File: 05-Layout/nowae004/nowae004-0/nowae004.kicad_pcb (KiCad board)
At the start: 2 copper layers, 150 x 68 mm, 801 parts, among them P1 SUPPLY IN, P2 MICROUSB, U2 FT230XS

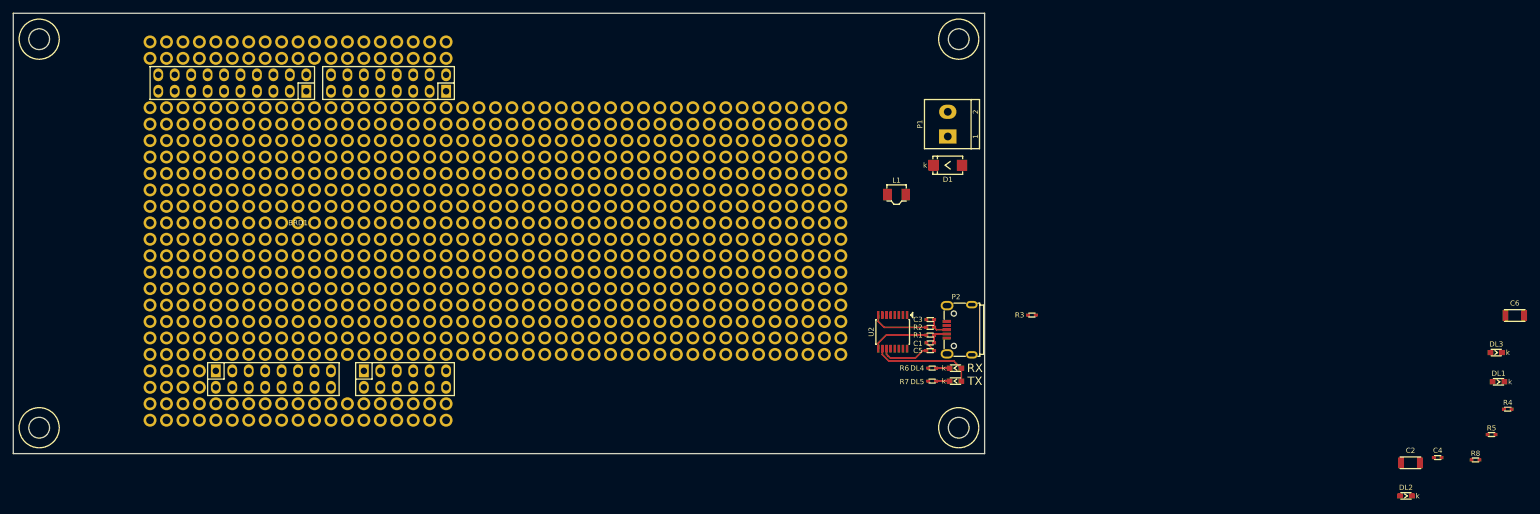
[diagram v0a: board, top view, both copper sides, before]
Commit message: NOWAE004: ended PCB development. TODO is fiducial, logos, license and hole in GND plane
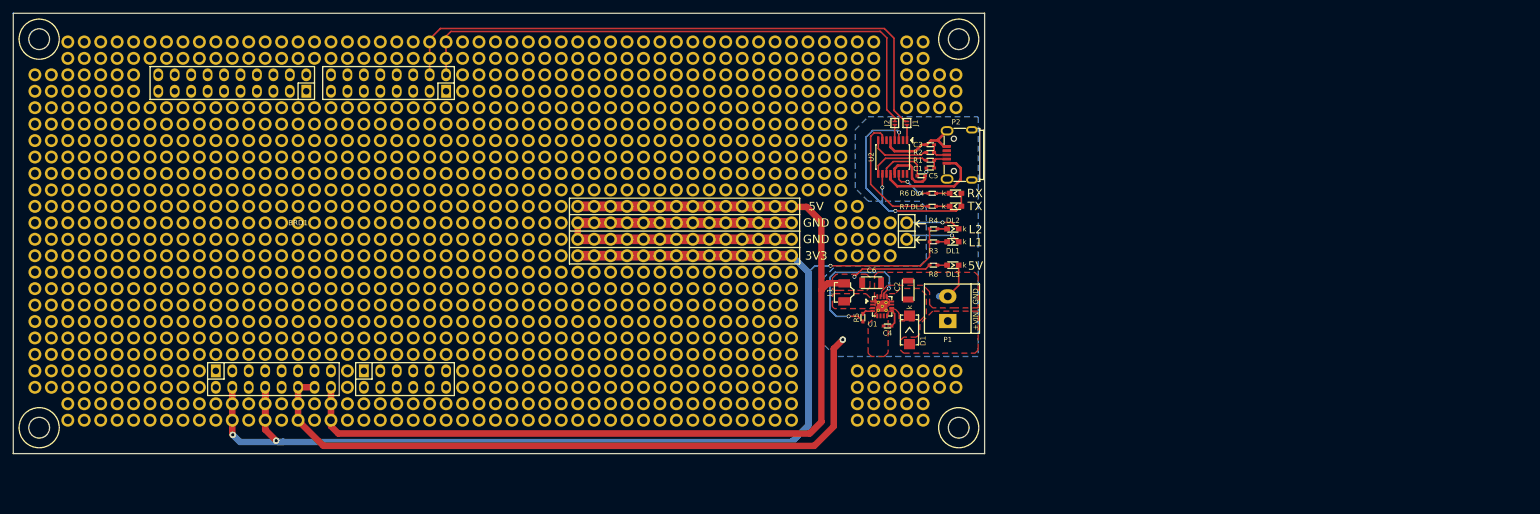
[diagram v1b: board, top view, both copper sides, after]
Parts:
- removed the VAL** at (177.8, 106.7)
- removed the VAL** at (177.8, 104.1)
- removed the VAL** at (177.8, 101.6)
- removed the VAL** at (177.8, 99.1)
- removed the VAL** at (177.8, 96.5)
- removed the VAL** at (177.8, 94.0)
- removed the VAL** at (175.3, 83.8)
- removed the VAL** at (175.3, 86.4)
- removed the VAL** at (175.3, 88.9)
- removed the VAL** at (175.3, 91.4)
- removed the VAL** at (175.3, 94.0)
- removed the VAL** at (175.3, 96.5)
- removed the VAL** at (175.3, 99.1)
- removed the VAL** at (175.3, 101.6)
- removed the VAL** at (175.3, 104.1)
- removed the VAL** at (175.3, 106.7)
- removed the VAL** at (172.7, 83.8)
- removed the VAL** at (172.7, 86.4)
- removed the VAL** at (172.7, 88.9)
- removed the VAL** at (172.7, 91.4)
- removed the VAL** at (172.7, 94.0)
- removed the VAL** at (172.7, 96.5)
- removed the VAL** at (172.7, 99.1)
- removed the VAL** at (172.7, 101.6)
- removed the VAL** at (172.7, 104.1)
- removed the VAL** at (172.7, 106.7)
- added J1: EN_SERIAL, MISC:JUMPERSMD-2, F.Cu at (188.0, 71.0)
- added J2: EN_SERIAL, MISC:JUMPERSMD-2, F.Cu at (186.1, 71.0)
- added P3: LED1, CONNECTOR:CONN-HOLE-1.2, F.Cu at (188.0, 88.9)
- added P4: LED2, CONNECTOR:CONN-HOLE-1.2, F.Cu at (188.0, 86.4)
- added U1: TPS62153, QFN:QFN16_3x3_0.5_16+1, F.Cu at (184.2, 99.2)
- added VAL**: CONN-HOLE-1.2, CONNECTOR:CONN-HOLE-1.2, F.Cu at (53.3, 106.7)
- added VAL**: CONN-HOLE-1.2, CONNECTOR:CONN-HOLE-1.2, F.Cu at (55.9, 106.7)
- added VAL**: CONN-HOLE-1.2, CONNECTOR:CONN-HOLE-1.2, F.Cu at (61.0, 91.4)
- added VAL**: CONN-HOLE-1.2, CONNECTOR:CONN-HOLE-1.2, F.Cu at (63.5, 86.4)
- added VAL**: CONN-HOLE-1.2, CONNECTOR:CONN-HOLE-1.2, F.Cu at (61.0, 88.9)
- added VAL**: CONN-HOLE-1.2, CONNECTOR:CONN-HOLE-1.2, F.Cu at (63.5, 88.9)
- added VAL**: CONN-HOLE-1.2, CONNECTOR:CONN-HOLE-1.2, F.Cu at (63.5, 91.4)
- added VAL**: CONN-HOLE-1.2, CONNECTOR:CONN-HOLE-1.2, F.Cu at (66.0, 86.4)
- added VAL**: CONN-HOLE-1.2, CONNECTOR:CONN-HOLE-1.2, F.Cu at (68.6, 88.9)
- added VAL**: CONN-HOLE-1.2, CONNECTOR:CONN-HOLE-1.2, F.Cu at (66.0, 91.4)
- added VAL**: CONN-HOLE-1.2, CONNECTOR:CONN-HOLE-1.2, F.Cu at (66.0, 88.9)
- added VAL**: CONN-HOLE-1.2, CONNECTOR:CONN-HOLE-1.2, F.Cu at (68.6, 86.4)
- added VAL**: CONN-HOLE-1.2, CONNECTOR:CONN-HOLE-1.2, F.Cu at (55.9, 94.0)
- added VAL**: CONN-HOLE-1.2, CONNECTOR:CONN-HOLE-1.2, F.Cu at (68.6, 91.4)
- added VAL**: CONN-HOLE-1.2, CONNECTOR:CONN-HOLE-1.2, F.Cu at (68.6, 94.0)
- added VAL**: CONN-HOLE-1.2, CONNECTOR:CONN-HOLE-1.2, F.Cu at (61.0, 94.0)
- added VAL**: CONN-HOLE-1.2, CONNECTOR:CONN-HOLE-1.2, F.Cu at (63.5, 94.0)
- added VAL**: CONN-HOLE-1.2, CONNECTOR:CONN-HOLE-1.2, F.Cu at (66.0, 94.0)
- added VAL**: CONN-HOLE-1.2, CONNECTOR:CONN-HOLE-1.2, F.Cu at (61.0, 104.1)
- added VAL**: CONN-HOLE-1.2, CONNECTOR:CONN-HOLE-1.2, F.Cu at (63.5, 101.6)
- added VAL**: CONN-HOLE-1.2, CONNECTOR:CONN-HOLE-1.2, F.Cu at (63.5, 104.1)
- added VAL**: CONN-HOLE-1.2, CONNECTOR:CONN-HOLE-1.2, F.Cu at (66.0, 101.6)
- added VAL**: CONN-HOLE-1.2, CONNECTOR:CONN-HOLE-1.2, F.Cu at (58.4, 104.1)
- added VAL**: CONN-HOLE-1.2, CONNECTOR:CONN-HOLE-1.2, F.Cu at (55.9, 99.1)
- added VAL**: CONN-HOLE-1.2, CONNECTOR:CONN-HOLE-1.2, F.Cu at (58.4, 99.1)
- added VAL**: CONN-HOLE-1.2, CONNECTOR:CONN-HOLE-1.2, F.Cu at (58.4, 101.6)
- added VAL**: CONN-HOLE-1.2, CONNECTOR:CONN-HOLE-1.2, F.Cu at (58.4, 94.0)
- added VAL**: CONN-HOLE-1.2, CONNECTOR:CONN-HOLE-1.2, F.Cu at (58.4, 96.5)
- added VAL**: CONN-HOLE-1.2, CONNECTOR:CONN-HOLE-1.2, F.Cu at (61.0, 96.5)
- added VAL**: CONN-HOLE-1.2, CONNECTOR:CONN-HOLE-1.2, F.Cu at (63.5, 96.5)
- added VAL**: CONN-HOLE-1.2, CONNECTOR:CONN-HOLE-1.2, F.Cu at (66.0, 96.5)
- added VAL**: CONN-HOLE-1.2, CONNECTOR:CONN-HOLE-1.2, F.Cu at (66.0, 99.1)
- added VAL**: CONN-HOLE-1.2, CONNECTOR:CONN-HOLE-1.2, F.Cu at (63.5, 99.1)
- added VAL**: CONN-HOLE-1.2, CONNECTOR:CONN-HOLE-1.2, F.Cu at (68.6, 101.6)
- added VAL**: CONN-HOLE-1.2, CONNECTOR:CONN-HOLE-1.2, F.Cu at (55.9, 96.5)
- added VAL**: CONN-HOLE-1.2, CONNECTOR:CONN-HOLE-1.2, F.Cu at (68.6, 99.1)
- added VAL**: CONN-HOLE-1.2, CONNECTOR:CONN-HOLE-1.2, F.Cu at (68.6, 96.5)
- added VAL**: CONN-HOLE-1.2, CONNECTOR:CONN-HOLE-1.2, F.Cu at (68.6, 104.1)
- added VAL**: CONN-HOLE-1.2, CONNECTOR:CONN-HOLE-1.2, F.Cu at (66.0, 106.7)
- added VAL**: CONN-HOLE-1.2, CONNECTOR:CONN-HOLE-1.2, F.Cu at (66.0, 104.1)
- added VAL**: CONN-HOLE-1.2, CONNECTOR:CONN-HOLE-1.2, F.Cu at (61.0, 101.6)
- added VAL**: CONN-HOLE-1.2, CONNECTOR:CONN-HOLE-1.2, F.Cu at (61.0, 99.1)
- added VAL**: CONN-HOLE-1.2, CONNECTOR:CONN-HOLE-1.2, F.Cu at (58.4, 109.2)
- added VAL**: CONN-HOLE-1.2, CONNECTOR:CONN-HOLE-1.2, F.Cu at (61.0, 109.2)
- added VAL**: CONN-HOLE-1.2, CONNECTOR:CONN-HOLE-1.2, F.Cu at (68.6, 106.7)
- added VAL**: CONN-HOLE-1.2, CONNECTOR:CONN-HOLE-1.2, F.Cu at (55.9, 101.6)
- added VAL**: CONN-HOLE-1.2, CONNECTOR:CONN-HOLE-1.2, F.Cu at (68.6, 109.2)
- added VAL**: CONN-HOLE-1.2, CONNECTOR:CONN-HOLE-1.2, F.Cu at (61.0, 106.7)
- added VAL**: CONN-HOLE-1.2, CONNECTOR:CONN-HOLE-1.2, F.Cu at (58.4, 106.7)
- added VAL**: CONN-HOLE-1.2, CONNECTOR:CONN-HOLE-1.2, F.Cu at (63.5, 106.7)
- added VAL**: CONN-HOLE-1.2, CONNECTOR:CONN-HOLE-1.2, F.Cu at (66.0, 109.2)
- added VAL**: CONN-HOLE-1.2, CONNECTOR:CONN-HOLE-1.2, F.Cu at (63.5, 109.2)
- added VAL**: CONN-HOLE-1.2, CONNECTOR:CONN-HOLE-1.2, F.Cu at (61.0, 111.8)
- added VAL**: CONN-HOLE-1.2, CONNECTOR:CONN-HOLE-1.2, F.Cu at (58.4, 111.8)
- added VAL**: CONN-HOLE-1.2, CONNECTOR:CONN-HOLE-1.2, F.Cu at (58.4, 114.3)
- added VAL**: CONN-HOLE-1.2, CONNECTOR:CONN-HOLE-1.2, F.Cu at (58.4, 116.8)
- added VAL**: CONN-HOLE-1.2, CONNECTOR:CONN-HOLE-1.2, F.Cu at (55.9, 109.2)
- added VAL**: CONN-HOLE-1.2, CONNECTOR:CONN-HOLE-1.2, F.Cu at (61.0, 116.8)
- added VAL**: CONN-HOLE-1.2, CONNECTOR:CONN-HOLE-1.2, F.Cu at (63.5, 111.8)
- added VAL**: CONN-HOLE-1.2, CONNECTOR:CONN-HOLE-1.2, F.Cu at (61.0, 114.3)
- added VAL**: CONN-HOLE-1.2, CONNECTOR:CONN-HOLE-1.2, F.Cu at (63.5, 114.3)
- added VAL**: CONN-HOLE-1.2, CONNECTOR:CONN-HOLE-1.2, F.Cu at (63.5, 116.8)
- added VAL**: CONN-HOLE-1.2, CONNECTOR:CONN-HOLE-1.2, F.Cu at (66.0, 111.8)
- added VAL**: CONN-HOLE-1.2, CONNECTOR:CONN-HOLE-1.2, F.Cu at (68.6, 114.3)
- added VAL**: CONN-HOLE-1.2, CONNECTOR:CONN-HOLE-1.2, F.Cu at (66.0, 116.8)
- added VAL**: CONN-HOLE-1.2, CONNECTOR:CONN-HOLE-1.2, F.Cu at (66.0, 114.3)
- added VAL**: CONN-HOLE-1.2, CONNECTOR:CONN-HOLE-1.2, F.Cu at (68.6, 111.8)
- added VAL**: CONN-HOLE-1.2, CONNECTOR:CONN-HOLE-1.2, F.Cu at (55.9, 111.8)
- added VAL**: CONN-HOLE-1.2, CONNECTOR:CONN-HOLE-1.2, F.Cu at (68.6, 116.8)
- added VAL**: CONN-HOLE-1.2, CONNECTOR:CONN-HOLE-1.2, F.Cu at (180.3, 91.4)
- added VAL**: CONN-HOLE-1.2, CONNECTOR:CONN-HOLE-1.2, F.Cu at (182.9, 91.4)
- added VAL**: CONN-HOLE-1.2, CONNECTOR:CONN-HOLE-1.2, F.Cu at (185.4, 91.4)
- added VAL**: CONN-HOLE-1.2, CONNECTOR:CONN-HOLE-1.2, F.Cu at (193.0, 63.5)
- added VAL**: CONN-HOLE-1.2, CONNECTOR:CONN-HOLE-1.2, F.Cu at (195.6, 68.6)
- added VAL**: CONN-HOLE-1.2, CONNECTOR:CONN-HOLE-1.2, F.Cu at (193.0, 66.0)
- added VAL**: CONN-HOLE-1.2, CONNECTOR:CONN-HOLE-1.2, F.Cu at (195.6, 66.0)
- added VAL**: CONN-HOLE-1.2, CONNECTOR:CONN-HOLE-1.2, F.Cu at (193.0, 68.6)
- added VAL**: CONN-HOLE-1.2, CONNECTOR:CONN-HOLE-1.2, F.Cu at (53.3, 88.9)
- added VAL**: CONN-HOLE-1.2, CONNECTOR:CONN-HOLE-1.2, F.Cu at (195.6, 63.5)
- added VAL**: CONN-HOLE-1.2, CONNECTOR:CONN-HOLE-1.2, F.Cu at (188.0, 58.4)
- added VAL**: CONN-HOLE-1.2, CONNECTOR:CONN-HOLE-1.2, F.Cu at (190.5, 58.4)
- added VAL**: CONN-HOLE-1.2, CONNECTOR:CONN-HOLE-1.2, F.Cu at (188.0, 61.0)
- added VAL**: CONN-HOLE-1.2, CONNECTOR:CONN-HOLE-1.2, F.Cu at (190.5, 61.0)
- added VAL**: CONN-HOLE-1.2, CONNECTOR:CONN-HOLE-1.2, F.Cu at (188.0, 63.5)
- added VAL**: CONN-HOLE-1.2, CONNECTOR:CONN-HOLE-1.2, F.Cu at (190.5, 68.6)
- added VAL**: CONN-HOLE-1.2, CONNECTOR:CONN-HOLE-1.2, F.Cu at (188.0, 66.0)
- added VAL**: CONN-HOLE-1.2, CONNECTOR:CONN-HOLE-1.2, F.Cu at (190.5, 66.0)
- added VAL**: CONN-HOLE-1.2, CONNECTOR:CONN-HOLE-1.2, F.Cu at (188.0, 68.6)
- added VAL**: CONN-HOLE-1.2, CONNECTOR:CONN-HOLE-1.2, F.Cu at (53.3, 91.4)
- added VAL**: CONN-HOLE-1.2, CONNECTOR:CONN-HOLE-1.2, F.Cu at (190.5, 63.5)
- added VAL**: CONN-HOLE-1.2, CONNECTOR:CONN-HOLE-1.2, F.Cu at (180.3, 61.0)
- added VAL**: CONN-HOLE-1.2, CONNECTOR:CONN-HOLE-1.2, F.Cu at (180.3, 63.5)
- added VAL**: CONN-HOLE-1.2, CONNECTOR:CONN-HOLE-1.2, F.Cu at (182.9, 63.5)
- added VAL**: CONN-HOLE-1.2, CONNECTOR:CONN-HOLE-1.2, F.Cu at (182.9, 58.4)
- added VAL**: CONN-HOLE-1.2, CONNECTOR:CONN-HOLE-1.2, F.Cu at (180.3, 58.4)
- added VAL**: CONN-HOLE-1.2, CONNECTOR:CONN-HOLE-1.2, F.Cu at (182.9, 61.0)
- added VAL**: CONN-HOLE-1.2, CONNECTOR:CONN-HOLE-1.2, F.Cu at (180.3, 66.0)
- added VAL**: CONN-HOLE-1.2, CONNECTOR:CONN-HOLE-1.2, F.Cu at (182.9, 68.6)
- added VAL**: CONN-HOLE-1.2, CONNECTOR:CONN-HOLE-1.2, F.Cu at (182.9, 66.0)
- added VAL**: CONN-HOLE-1.2, CONNECTOR:CONN-HOLE-1.2, F.Cu at (53.3, 81.3)
- added VAL**: CONN-HOLE-1.2, CONNECTOR:CONN-HOLE-1.2, F.Cu at (180.3, 68.6)
- added VAL**: CONN-HOLE-1.2, CONNECTOR:CONN-HOLE-1.2, F.Cu at (172.7, 58.4)
- added VAL**: CONN-HOLE-1.2, CONNECTOR:CONN-HOLE-1.2, F.Cu at (172.7, 61.0)
- added VAL**: CONN-HOLE-1.2, CONNECTOR:CONN-HOLE-1.2, F.Cu at (177.8, 58.4)
- added VAL**: CONN-HOLE-1.2, CONNECTOR:CONN-HOLE-1.2, F.Cu at (175.3, 61.0)
- added VAL**: CONN-HOLE-1.2, CONNECTOR:CONN-HOLE-1.2, F.Cu at (177.8, 61.0)
- added VAL**: CONN-HOLE-1.2, CONNECTOR:CONN-HOLE-1.2, F.Cu at (175.3, 58.4)
- added VAL**: CONN-HOLE-1.2, CONNECTOR:CONN-HOLE-1.2, F.Cu at (175.3, 63.5)
- added VAL**: CONN-HOLE-1.2, CONNECTOR:CONN-HOLE-1.2, F.Cu at (172.7, 63.5)
- added VAL**: CONN-HOLE-1.2, CONNECTOR:CONN-HOLE-1.2, F.Cu at (177.8, 63.5)
- added VAL**: CONN-HOLE-1.2, CONNECTOR:CONN-HOLE-1.2, F.Cu at (53.3, 104.1)
- added VAL**: CONN-HOLE-1.2, CONNECTOR:CONN-HOLE-1.2, F.Cu at (53.3, 78.7)
- added VAL**: CONN-HOLE-1.2, CONNECTOR:CONN-HOLE-1.2, F.Cu at (175.3, 66.0)
- added VAL**: CONN-HOLE-1.2, CONNECTOR:CONN-HOLE-1.2, F.Cu at (177.8, 66.0)
- added VAL**: CONN-HOLE-1.2, CONNECTOR:CONN-HOLE-1.2, F.Cu at (172.7, 66.0)
- added VAL**: CONN-HOLE-1.2, CONNECTOR:CONN-HOLE-1.2, F.Cu at (53.3, 76.2)
- added VAL**: CONN-HOLE-1.2, CONNECTOR:CONN-HOLE-1.2, F.Cu at (185.4, 86.4)
- added VAL**: CONN-HOLE-1.2, CONNECTOR:CONN-HOLE-1.2, F.Cu at (53.3, 86.4)
- added VAL**: CONN-HOLE-1.2, CONNECTOR:CONN-HOLE-1.2, F.Cu at (185.4, 88.9)
- added VAL**: CONN-HOLE-1.2, CONNECTOR:CONN-HOLE-1.2, F.Cu at (182.9, 88.9)
- added VAL**: CONN-HOLE-1.2, CONNECTOR:CONN-HOLE-1.2, F.Cu at (180.3, 83.8)
- added VAL**: CONN-HOLE-1.2, CONNECTOR:CONN-HOLE-1.2, F.Cu at (180.3, 86.4)
- added VAL**: CONN-HOLE-1.2, CONNECTOR:CONN-HOLE-1.2, F.Cu at (180.3, 88.9)
- added VAL**: CONN-HOLE-1.2, CONNECTOR:CONN-HOLE-1.2, F.Cu at (182.9, 86.4)
- added VAL**: CONN-HOLE-1.2, CONNECTOR:CONN-HOLE-1.2, F.Cu at (53.3, 83.8)
- added VAL**: CONN-HOLE-1.2, CONNECTOR:CONN-HOLE-1.2, F.Cu at (190.5, 114.3)
- added VAL**: CONN-HOLE-1.2, CONNECTOR:CONN-HOLE-1.2, F.Cu at (188.0, 116.8)
- added VAL**: CONN-HOLE-1.2, CONNECTOR:CONN-HOLE-1.2, F.Cu at (190.5, 116.8)
- added VAL**: CONN-HOLE-1.2, CONNECTOR:CONN-HOLE-1.2, F.Cu at (185.4, 116.8)
- added VAL**: CONN-HOLE-1.2, CONNECTOR:CONN-HOLE-1.2, F.Cu at (182.9, 114.3)
- added VAL**: CONN-HOLE-1.2, CONNECTOR:CONN-HOLE-1.2, F.Cu at (182.9, 109.2)
- added VAL**: CONN-HOLE-1.2, CONNECTOR:CONN-HOLE-1.2, F.Cu at (180.3, 116.8)
- added VAL**: CONN-HOLE-1.2, CONNECTOR:CONN-HOLE-1.2, F.Cu at (180.3, 114.3)
- added VAL**: CONN-HOLE-1.2, CONNECTOR:CONN-HOLE-1.2, F.Cu at (180.3, 111.8)
- added VAL**: CONN-HOLE-1.2, CONNECTOR:CONN-HOLE-1.2, F.Cu at (53.3, 73.7)
- added VAL**: CONN-HOLE-1.2, CONNECTOR:CONN-HOLE-1.2, F.Cu at (182.9, 116.8)
- added VAL**: CONN-HOLE-1.2, CONNECTOR:CONN-HOLE-1.2, F.Cu at (180.3, 109.2)
- added VAL**: CONN-HOLE-1.2, CONNECTOR:CONN-HOLE-1.2, F.Cu at (182.9, 111.8)
- added VAL**: CONN-HOLE-1.2, CONNECTOR:CONN-HOLE-1.2, F.Cu at (185.4, 114.3)
- added VAL**: CONN-HOLE-1.2, CONNECTOR:CONN-HOLE-1.2, F.Cu at (188.0, 111.8)
- added VAL**: CONN-HOLE-1.2, CONNECTOR:CONN-HOLE-1.2, F.Cu at (185.4, 111.8)
- added VAL**: CONN-HOLE-1.2, CONNECTOR:CONN-HOLE-1.2, F.Cu at (190.5, 111.8)
- added VAL**: CONN-HOLE-1.2, CONNECTOR:CONN-HOLE-1.2, F.Cu at (188.0, 114.3)
- added VAL**: CONN-HOLE-1.2, CONNECTOR:CONN-HOLE-1.2, F.Cu at (185.4, 109.2)
- added VAL**: CONN-HOLE-1.2, CONNECTOR:CONN-HOLE-1.2, F.Cu at (188.0, 109.2)
- added VAL**: CONN-HOLE-1.2, CONNECTOR:CONN-HOLE-1.2, F.Cu at (53.3, 68.6)
- added VAL**: CONN-HOLE-1.2, CONNECTOR:CONN-HOLE-1.2, F.Cu at (190.5, 109.2)
- added VAL**: CONN-HOLE-1.2, CONNECTOR:CONN-HOLE-1.2, F.Cu at (195.6, 111.8)
- added VAL**: CONN-HOLE-1.2, CONNECTOR:CONN-HOLE-1.2, F.Cu at (193.0, 111.8)
- added VAL**: CONN-HOLE-1.2, CONNECTOR:CONN-HOLE-1.2, F.Cu at (195.6, 109.2)
- added VAL**: CONN-HOLE-1.2, CONNECTOR:CONN-HOLE-1.2, F.Cu at (193.0, 109.2)
- added VAL**: CONN-HOLE-1.2, CONNECTOR:CONN-HOLE-1.2, F.Cu at (132.1, 109.2)
- added VAL**: CONN-HOLE-1.2, CONNECTOR:CONN-HOLE-1.2, F.Cu at (127.0, 114.3)
- added VAL**: CONN-HOLE-1.2, CONNECTOR:CONN-HOLE-1.2, F.Cu at (127.0, 111.8)
- added VAL**: CONN-HOLE-1.2, CONNECTOR:CONN-HOLE-1.2, F.Cu at (127.0, 109.2)
- added VAL**: CONN-HOLE-1.2, CONNECTOR:CONN-HOLE-1.2, F.Cu at (129.5, 109.2)
- added VAL**: CONN-HOLE-1.2, CONNECTOR:CONN-HOLE-1.2, F.Cu at (53.3, 71.1)
- added VAL**: CONN-HOLE-1.2, CONNECTOR:CONN-HOLE-1.2, F.Cu at (134.6, 116.8)
- added VAL**: CONN-HOLE-1.2, CONNECTOR:CONN-HOLE-1.2, F.Cu at (127.0, 116.8)
- added VAL**: CONN-HOLE-1.2, CONNECTOR:CONN-HOLE-1.2, F.Cu at (134.6, 114.3)
- added VAL**: CONN-HOLE-1.2, CONNECTOR:CONN-HOLE-1.2, F.Cu at (134.6, 111.8)
- added VAL**: CONN-HOLE-1.2, CONNECTOR:CONN-HOLE-1.2, F.Cu at (134.6, 109.2)
- added VAL**: CONN-HOLE-1.2, CONNECTOR:CONN-HOLE-1.2, F.Cu at (121.9, 116.8)
- added VAL**: CONN-HOLE-1.2, CONNECTOR:CONN-HOLE-1.2, F.Cu at (119.4, 116.8)
- added VAL**: CONN-HOLE-1.2, CONNECTOR:CONN-HOLE-1.2, F.Cu at (124.5, 116.8)
- added VAL**: CONN-HOLE-1.2, CONNECTOR:CONN-HOLE-1.2, F.Cu at (124.5, 114.3)
- added VAL**: CONN-HOLE-1.2, CONNECTOR:CONN-HOLE-1.2, F.Cu at (119.4, 114.3)
- added VAL**: CONN-HOLE-1.2, CONNECTOR:CONN-HOLE-1.2, F.Cu at (55.9, 78.7)
- added VAL**: CONN-HOLE-1.2, CONNECTOR:CONN-HOLE-1.2, F.Cu at (121.9, 114.3)
- added VAL**: CONN-HOLE-1.2, CONNECTOR:CONN-HOLE-1.2, F.Cu at (132.1, 111.8)
- added VAL**: CONN-HOLE-1.2, CONNECTOR:CONN-HOLE-1.2, F.Cu at (129.5, 111.8)
- added VAL**: CONN-HOLE-1.2, CONNECTOR:CONN-HOLE-1.2, F.Cu at (129.5, 116.8)
- added VAL**: CONN-HOLE-1.2, CONNECTOR:CONN-HOLE-1.2, F.Cu at (132.1, 114.3)
- added VAL**: CONN-HOLE-1.2, CONNECTOR:CONN-HOLE-1.2, F.Cu at (132.1, 116.8)
- added VAL**: CONN-HOLE-1.2, CONNECTOR:CONN-HOLE-1.2, F.Cu at (129.5, 114.3)
- added VAL**: CONN-HOLE-1.2, CONNECTOR:CONN-HOLE-1.2, F.Cu at (162.6, 109.2)
- added VAL**: CONN-HOLE-1.2, CONNECTOR:CONN-HOLE-1.2, F.Cu at (162.6, 111.8)
- added VAL**: CONN-HOLE-1.2, CONNECTOR:CONN-HOLE-1.2, F.Cu at (165.1, 109.2)
- added VAL**: CONN-HOLE-1.2, CONNECTOR:CONN-HOLE-1.2, F.Cu at (55.9, 81.3)
- added VAL**: CONN-HOLE-1.2, CONNECTOR:CONN-HOLE-1.2, F.Cu at (165.1, 111.8)
- added VAL**: CONN-HOLE-1.2, CONNECTOR:CONN-HOLE-1.2, F.Cu at (157.5, 109.2)
- added VAL**: CONN-HOLE-1.2, CONNECTOR:CONN-HOLE-1.2, F.Cu at (160.0, 109.2)
- added VAL**: CONN-HOLE-1.2, CONNECTOR:CONN-HOLE-1.2, F.Cu at (154.9, 109.2)
- added VAL**: CONN-HOLE-1.2, CONNECTOR:CONN-HOLE-1.2, F.Cu at (157.5, 116.8)
- added VAL**: CONN-HOLE-1.2, CONNECTOR:CONN-HOLE-1.2, F.Cu at (157.5, 111.8)
- added VAL**: CONN-HOLE-1.2, CONNECTOR:CONN-HOLE-1.2, F.Cu at (152.4, 116.8)
- added VAL**: CONN-HOLE-1.2, CONNECTOR:CONN-HOLE-1.2, F.Cu at (152.4, 114.3)
- added VAL**: CONN-HOLE-1.2, CONNECTOR:CONN-HOLE-1.2, F.Cu at (154.9, 111.8)
- added VAL**: CONN-HOLE-1.2, CONNECTOR:CONN-HOLE-1.2, F.Cu at (154.9, 114.3)
- added VAL**: CONN-HOLE-1.2, CONNECTOR:CONN-HOLE-1.2, F.Cu at (55.9, 68.6)
- added VAL**: CONN-HOLE-1.2, CONNECTOR:CONN-HOLE-1.2, F.Cu at (154.9, 116.8)
- added VAL**: CONN-HOLE-1.2, CONNECTOR:CONN-HOLE-1.2, F.Cu at (157.5, 114.3)
- added VAL**: CONN-HOLE-1.2, CONNECTOR:CONN-HOLE-1.2, F.Cu at (165.1, 116.8)
- added VAL**: CONN-HOLE-1.2, CONNECTOR:CONN-HOLE-1.2, F.Cu at (165.1, 114.3)
- added VAL**: CONN-HOLE-1.2, CONNECTOR:CONN-HOLE-1.2, F.Cu at (160.0, 111.8)
- added VAL**: CONN-HOLE-1.2, CONNECTOR:CONN-HOLE-1.2, F.Cu at (162.6, 114.3)
- added VAL**: CONN-HOLE-1.2, CONNECTOR:CONN-HOLE-1.2, F.Cu at (162.6, 116.8)
- added VAL**: CONN-HOLE-1.2, CONNECTOR:CONN-HOLE-1.2, F.Cu at (160.0, 114.3)
- added VAL**: CONN-HOLE-1.2, CONNECTOR:CONN-HOLE-1.2, F.Cu at (160.0, 116.8)
- added VAL**: CONN-HOLE-1.2, CONNECTOR:CONN-HOLE-1.2, F.Cu at (149.9, 116.8)
- added VAL**: CONN-HOLE-1.2, CONNECTOR:CONN-HOLE-1.2, F.Cu at (53.3, 101.6)
- added VAL**: CONN-HOLE-1.2, CONNECTOR:CONN-HOLE-1.2, F.Cu at (55.9, 73.7)
- added VAL**: CONN-HOLE-1.2, CONNECTOR:CONN-HOLE-1.2, F.Cu at (147.3, 116.8)
- added VAL**: CONN-HOLE-1.2, CONNECTOR:CONN-HOLE-1.2, F.Cu at (149.9, 114.3)
- added VAL**: CONN-HOLE-1.2, CONNECTOR:CONN-HOLE-1.2, F.Cu at (144.8, 114.3)
- added VAL**: CONN-HOLE-1.2, CONNECTOR:CONN-HOLE-1.2, F.Cu at (144.8, 116.8)
- added VAL**: CONN-HOLE-1.2, CONNECTOR:CONN-HOLE-1.2, F.Cu at (147.3, 114.3)
- added VAL**: CONN-HOLE-1.2, CONNECTOR:CONN-HOLE-1.2, F.Cu at (147.3, 111.8)
- added VAL**: CONN-HOLE-1.2, CONNECTOR:CONN-HOLE-1.2, F.Cu at (142.2, 116.8)
- added VAL**: CONN-HOLE-1.2, CONNECTOR:CONN-HOLE-1.2, F.Cu at (142.2, 114.3)
- added VAL**: CONN-HOLE-1.2, CONNECTOR:CONN-HOLE-1.2, F.Cu at (142.2, 111.8)
- added VAL**: CONN-HOLE-1.2, CONNECTOR:CONN-HOLE-1.2, F.Cu at (144.8, 111.8)
- added VAL**: CONN-HOLE-1.2, CONNECTOR:CONN-HOLE-1.2, F.Cu at (55.9, 71.1)
- added VAL**: CONN-HOLE-1.2, CONNECTOR:CONN-HOLE-1.2, F.Cu at (139.7, 116.8)
- added VAL**: CONN-HOLE-1.2, CONNECTOR:CONN-HOLE-1.2, F.Cu at (137.2, 111.8)
- added VAL**: CONN-HOLE-1.2, CONNECTOR:CONN-HOLE-1.2, F.Cu at (137.2, 114.3)
- added VAL**: CONN-HOLE-1.2, CONNECTOR:CONN-HOLE-1.2, F.Cu at (137.2, 116.8)
- added VAL**: CONN-HOLE-1.2, CONNECTOR:CONN-HOLE-1.2, F.Cu at (139.7, 111.8)
- added VAL**: CONN-HOLE-1.2, CONNECTOR:CONN-HOLE-1.2, F.Cu at (139.7, 114.3)
- added VAL**: CONN-HOLE-1.2, CONNECTOR:CONN-HOLE-1.2, F.Cu at (149.9, 111.8)
- added VAL**: CONN-HOLE-1.2, CONNECTOR:CONN-HOLE-1.2, F.Cu at (152.4, 111.8)
- added VAL**: CONN-HOLE-1.2, CONNECTOR:CONN-HOLE-1.2, F.Cu at (152.4, 109.2)
- added VAL**: CONN-HOLE-1.2, CONNECTOR:CONN-HOLE-1.2, F.Cu at (149.9, 109.2)
- added VAL**: CONN-HOLE-1.2, CONNECTOR:CONN-HOLE-1.2, F.Cu at (55.9, 76.2)
- added VAL**: CONN-HOLE-1.2, CONNECTOR:CONN-HOLE-1.2, F.Cu at (137.2, 109.2)
- added VAL**: CONN-HOLE-1.2, CONNECTOR:CONN-HOLE-1.2, F.Cu at (147.3, 109.2)
- added VAL**: CONN-HOLE-1.2, CONNECTOR:CONN-HOLE-1.2, F.Cu at (139.7, 109.2)
- added VAL**: CONN-HOLE-1.2, CONNECTOR:CONN-HOLE-1.2, F.Cu at (142.2, 109.2)
- added VAL**: CONN-HOLE-1.2, CONNECTOR:CONN-HOLE-1.2, F.Cu at (144.8, 109.2)
- added VAL**: CONN-HOLE-1.2, CONNECTOR:CONN-HOLE-1.2, F.Cu at (119.4, 109.2)
- added VAL**: CONN-HOLE-1.2, CONNECTOR:CONN-HOLE-1.2, F.Cu at (119.4, 111.8)
- added VAL**: CONN-HOLE-1.2, CONNECTOR:CONN-HOLE-1.2, F.Cu at (121.9, 111.8)
- added VAL**: CONN-HOLE-1.2, CONNECTOR:CONN-HOLE-1.2, F.Cu at (124.5, 111.8)
- added VAL**: CONN-HOLE-1.2, CONNECTOR:CONN-HOLE-1.2, F.Cu at (124.5, 109.2)
- added VAL**: CONN-HOLE-1.2, CONNECTOR:CONN-HOLE-1.2, F.Cu at (55.9, 88.9)
- added VAL**: CONN-HOLE-1.2, CONNECTOR:CONN-HOLE-1.2, F.Cu at (121.9, 109.2)
- added VAL**: CONN-HOLE-1.2, CONNECTOR:CONN-HOLE-1.2, F.Cu at (167.6, 116.8)
- added VAL**: CONN-HOLE-1.2, CONNECTOR:CONN-HOLE-1.2, F.Cu at (170.2, 111.8)
- added VAL**: CONN-HOLE-1.2, CONNECTOR:CONN-HOLE-1.2, F.Cu at (170.2, 114.3)
- added VAL**: CONN-HOLE-1.2, CONNECTOR:CONN-HOLE-1.2, F.Cu at (170.2, 116.8)
- added VAL**: CONN-HOLE-1.2, CONNECTOR:CONN-HOLE-1.2, F.Cu at (167.6, 111.8)
- added VAL**: CONN-HOLE-1.2, CONNECTOR:CONN-HOLE-1.2, F.Cu at (167.6, 114.3)
- added VAL**: CONN-HOLE-1.2, CONNECTOR:CONN-HOLE-1.2, F.Cu at (167.6, 109.2)
- added VAL**: CONN-HOLE-1.2, CONNECTOR:CONN-HOLE-1.2, F.Cu at (170.2, 109.2)
- added VAL**: CONN-HOLE-1.2, CONNECTOR:CONN-HOLE-1.2, F.Cu at (132.1, 66.0)
- added VAL**: CONN-HOLE-1.2, CONNECTOR:CONN-HOLE-1.2, F.Cu at (55.9, 83.8)
- added VAL**: CONN-HOLE-1.2, CONNECTOR:CONN-HOLE-1.2, F.Cu at (160.0, 61.0)
- added VAL**: CONN-HOLE-1.2, CONNECTOR:CONN-HOLE-1.2, F.Cu at (160.0, 63.5)
- added VAL**: CONN-HOLE-1.2, CONNECTOR:CONN-HOLE-1.2, F.Cu at (162.6, 61.0)
- added VAL**: CONN-HOLE-1.2, CONNECTOR:CONN-HOLE-1.2, F.Cu at (162.6, 63.5)
- added VAL**: CONN-HOLE-1.2, CONNECTOR:CONN-HOLE-1.2, F.Cu at (160.0, 58.4)
- added VAL**: CONN-HOLE-1.2, CONNECTOR:CONN-HOLE-1.2, F.Cu at (154.9, 66.0)
- added VAL**: CONN-HOLE-1.2, CONNECTOR:CONN-HOLE-1.2, F.Cu at (152.4, 66.0)
- added VAL**: CONN-HOLE-1.2, CONNECTOR:CONN-HOLE-1.2, F.Cu at (152.4, 63.5)
- added VAL**: CONN-HOLE-1.2, CONNECTOR:CONN-HOLE-1.2, F.Cu at (154.9, 63.5)
- added VAL**: CONN-HOLE-1.2, CONNECTOR:CONN-HOLE-1.2, F.Cu at (157.5, 63.5)
- added VAL**: CONN-HOLE-1.2, CONNECTOR:CONN-HOLE-1.2, F.Cu at (55.9, 86.4)
- added VAL**: CONN-HOLE-1.2, CONNECTOR:CONN-HOLE-1.2, F.Cu at (157.5, 61.0)
- added VAL**: CONN-HOLE-1.2, CONNECTOR:CONN-HOLE-1.2, F.Cu at (157.5, 58.4)
- added VAL**: CONN-HOLE-1.2, CONNECTOR:CONN-HOLE-1.2, F.Cu at (152.4, 61.0)
- added VAL**: CONN-HOLE-1.2, CONNECTOR:CONN-HOLE-1.2, F.Cu at (152.4, 58.4)
- added VAL**: CONN-HOLE-1.2, CONNECTOR:CONN-HOLE-1.2, F.Cu at (154.9, 58.4)
- added VAL**: CONN-HOLE-1.2, CONNECTOR:CONN-HOLE-1.2, F.Cu at (154.9, 61.0)
- added VAL**: CONN-HOLE-1.2, CONNECTOR:CONN-HOLE-1.2, F.Cu at (165.1, 66.0)
- added VAL**: CONN-HOLE-1.2, CONNECTOR:CONN-HOLE-1.2, F.Cu at (165.1, 63.5)
- added VAL**: CONN-HOLE-1.2, CONNECTOR:CONN-HOLE-1.2, F.Cu at (165.1, 61.0)
- added VAL**: CONN-HOLE-1.2, CONNECTOR:CONN-HOLE-1.2, F.Cu at (165.1, 58.4)
- added VAL**: CONN-HOLE-1.2, CONNECTOR:CONN-HOLE-1.2, F.Cu at (55.9, 91.4)
- added VAL**: CONN-HOLE-1.2, CONNECTOR:CONN-HOLE-1.2, F.Cu at (162.6, 58.4)
- added VAL**: CONN-HOLE-1.2, CONNECTOR:CONN-HOLE-1.2, F.Cu at (162.6, 66.0)
- added VAL**: CONN-HOLE-1.2, CONNECTOR:CONN-HOLE-1.2, F.Cu at (160.0, 66.0)
- added VAL**: CONN-HOLE-1.2, CONNECTOR:CONN-HOLE-1.2, F.Cu at (157.5, 66.0)
- added VAL**: CONN-HOLE-1.2, CONNECTOR:CONN-HOLE-1.2, F.Cu at (147.3, 66.0)
- added VAL**: CONN-HOLE-1.2, CONNECTOR:CONN-HOLE-1.2, F.Cu at (149.9, 66.0)
- added VAL**: CONN-HOLE-1.2, CONNECTOR:CONN-HOLE-1.2, F.Cu at (142.2, 66.0)
- added VAL**: CONN-HOLE-1.2, CONNECTOR:CONN-HOLE-1.2, F.Cu at (144.8, 66.0)
- added VAL**: CONN-HOLE-1.2, CONNECTOR:CONN-HOLE-1.2, F.Cu at (142.2, 63.5)
- added VAL**: CONN-HOLE-1.2, CONNECTOR:CONN-HOLE-1.2, F.Cu at (142.2, 61.0)
- added VAL**: CONN-HOLE-1.2, CONNECTOR:CONN-HOLE-1.2, F.Cu at (53.3, 66.0)
- added VAL**: CONN-HOLE-1.2, CONNECTOR:CONN-HOLE-1.2, F.Cu at (142.2, 58.4)
- added VAL**: CONN-HOLE-1.2, CONNECTOR:CONN-HOLE-1.2, F.Cu at (144.8, 58.4)
- added VAL**: CONN-HOLE-1.2, CONNECTOR:CONN-HOLE-1.2, F.Cu at (144.8, 61.0)
- added VAL**: CONN-HOLE-1.2, CONNECTOR:CONN-HOLE-1.2, F.Cu at (144.8, 63.5)
- added VAL**: CONN-HOLE-1.2, CONNECTOR:CONN-HOLE-1.2, F.Cu at (137.2, 66.0)
- added VAL**: CONN-HOLE-1.2, CONNECTOR:CONN-HOLE-1.2, F.Cu at (139.7, 66.0)
- added VAL**: CONN-HOLE-1.2, CONNECTOR:CONN-HOLE-1.2, F.Cu at (139.7, 63.5)
- added VAL**: CONN-HOLE-1.2, CONNECTOR:CONN-HOLE-1.2, F.Cu at (139.7, 58.4)
- added VAL**: CONN-HOLE-1.2, CONNECTOR:CONN-HOLE-1.2, F.Cu at (137.2, 58.4)
- added VAL**: CONN-HOLE-1.2, CONNECTOR:CONN-HOLE-1.2, F.Cu at (137.2, 61.0)
- added VAL**: CONN-HOLE-1.2, CONNECTOR:CONN-HOLE-1.2, F.Cu at (55.9, 66.0)
- added VAL**: CONN-HOLE-1.2, CONNECTOR:CONN-HOLE-1.2, F.Cu at (137.2, 63.5)
- added VAL**: CONN-HOLE-1.2, CONNECTOR:CONN-HOLE-1.2, F.Cu at (139.7, 61.0)
- added VAL**: CONN-HOLE-1.2, CONNECTOR:CONN-HOLE-1.2, F.Cu at (149.9, 63.5)
- added VAL**: CONN-HOLE-1.2, CONNECTOR:CONN-HOLE-1.2, F.Cu at (149.9, 58.4)
- added VAL**: CONN-HOLE-1.2, CONNECTOR:CONN-HOLE-1.2, F.Cu at (147.3, 58.4)
- added VAL**: CONN-HOLE-1.2, CONNECTOR:CONN-HOLE-1.2, F.Cu at (147.3, 61.0)
- added VAL**: CONN-HOLE-1.2, CONNECTOR:CONN-HOLE-1.2, F.Cu at (147.3, 63.5)
- added VAL**: CONN-HOLE-1.2, CONNECTOR:CONN-HOLE-1.2, F.Cu at (149.9, 61.0)
- added VAL**: CONN-HOLE-1.2, CONNECTOR:CONN-HOLE-1.2, F.Cu at (134.6, 66.0)
- added VAL**: CONN-HOLE-1.2, CONNECTOR:CONN-HOLE-1.2, F.Cu at (121.9, 61.0)
- added VAL**: CONN-HOLE-1.2, CONNECTOR:CONN-HOLE-1.2, F.Cu at (63.5, 66.0)
- added VAL**: CONN-HOLE-1.2, CONNECTOR:CONN-HOLE-1.2, F.Cu at (119.4, 58.4)
- added VAL**: CONN-HOLE-1.2, CONNECTOR:CONN-HOLE-1.2, F.Cu at (119.4, 61.0)
- added VAL**: CONN-HOLE-1.2, CONNECTOR:CONN-HOLE-1.2, F.Cu at (124.5, 61.0)
- added VAL**: CONN-HOLE-1.2, CONNECTOR:CONN-HOLE-1.2, F.Cu at (124.5, 58.4)
- added VAL**: CONN-HOLE-1.2, CONNECTOR:CONN-HOLE-1.2, F.Cu at (121.9, 58.4)
- added VAL**: CONN-HOLE-1.2, CONNECTOR:CONN-HOLE-1.2, F.Cu at (121.9, 66.0)
- added VAL**: CONN-HOLE-1.2, CONNECTOR:CONN-HOLE-1.2, F.Cu at (119.4, 63.5)
- added VAL**: CONN-HOLE-1.2, CONNECTOR:CONN-HOLE-1.2, F.Cu at (119.4, 66.0)
- added VAL**: CONN-HOLE-1.2, CONNECTOR:CONN-HOLE-1.2, F.Cu at (124.5, 66.0)
- added VAL**: CONN-HOLE-1.2, CONNECTOR:CONN-HOLE-1.2, F.Cu at (124.5, 63.5)
- added VAL**: CONN-HOLE-1.2, CONNECTOR:CONN-HOLE-1.2, F.Cu at (53.3, 111.8)
- added VAL**: CONN-HOLE-1.2, CONNECTOR:CONN-HOLE-1.2, F.Cu at (61.0, 61.0)
- added VAL**: CONN-HOLE-1.2, CONNECTOR:CONN-HOLE-1.2, F.Cu at (121.9, 63.5)
- added VAL**: CONN-HOLE-1.2, CONNECTOR:CONN-HOLE-1.2, F.Cu at (134.6, 63.5)
- added VAL**: CONN-HOLE-1.2, CONNECTOR:CONN-HOLE-1.2, F.Cu at (134.6, 58.4)
- added VAL**: CONN-HOLE-1.2, CONNECTOR:CONN-HOLE-1.2, F.Cu at (132.1, 58.4)
- added VAL**: CONN-HOLE-1.2, CONNECTOR:CONN-HOLE-1.2, F.Cu at (132.1, 61.0)
- added VAL**: CONN-HOLE-1.2, CONNECTOR:CONN-HOLE-1.2, F.Cu at (132.1, 63.5)
- added VAL**: CONN-HOLE-1.2, CONNECTOR:CONN-HOLE-1.2, F.Cu at (134.6, 61.0)
- added VAL**: CONN-HOLE-1.2, CONNECTOR:CONN-HOLE-1.2, F.Cu at (127.0, 66.0)
- added VAL**: CONN-HOLE-1.2, CONNECTOR:CONN-HOLE-1.2, F.Cu at (129.5, 63.5)
- added VAL**: CONN-HOLE-1.2, CONNECTOR:CONN-HOLE-1.2, F.Cu at (129.5, 66.0)
- added VAL**: CONN-HOLE-1.2, CONNECTOR:CONN-HOLE-1.2, F.Cu at (58.4, 63.5)
- added VAL**: CONN-HOLE-1.2, CONNECTOR:CONN-HOLE-1.2, F.Cu at (127.0, 63.5)
- added VAL**: CONN-HOLE-1.2, CONNECTOR:CONN-HOLE-1.2, F.Cu at (127.0, 61.0)
- added VAL**: CONN-HOLE-1.2, CONNECTOR:CONN-HOLE-1.2, F.Cu at (127.0, 58.4)
- added VAL**: CONN-HOLE-1.2, CONNECTOR:CONN-HOLE-1.2, F.Cu at (129.5, 58.4)
- added VAL**: CONN-HOLE-1.2, CONNECTOR:CONN-HOLE-1.2, F.Cu at (129.5, 61.0)
- added VAL**: CONN-HOLE-1.2, CONNECTOR:CONN-HOLE-1.2, F.Cu at (167.6, 63.5)
- added VAL**: CONN-HOLE-1.2, CONNECTOR:CONN-HOLE-1.2, F.Cu at (167.6, 58.4)
- added VAL**: CONN-HOLE-1.2, CONNECTOR:CONN-HOLE-1.2, F.Cu at (170.2, 58.4)
- added VAL**: CONN-HOLE-1.2, CONNECTOR:CONN-HOLE-1.2, F.Cu at (170.2, 61.0)
- added VAL**: CONN-HOLE-1.2, CONNECTOR:CONN-HOLE-1.2, F.Cu at (170.2, 63.5)
- added VAL**: CONN-HOLE-1.2, CONNECTOR:CONN-HOLE-1.2, F.Cu at (63.5, 61.0)
- added VAL**: CONN-HOLE-1.2, CONNECTOR:CONN-HOLE-1.2, F.Cu at (167.6, 61.0)
- added VAL**: CONN-HOLE-1.2, CONNECTOR:CONN-HOLE-1.2, F.Cu at (167.6, 66.0)
- added VAL**: CONN-HOLE-1.2, CONNECTOR:CONN-HOLE-1.2, F.Cu at (170.2, 66.0)
- added VAL**: CONN-HOLE-1.2, CONNECTOR:CONN-HOLE-1.2, F.Cu at (101.6, 111.8)
- added VAL**: CONN-HOLE-1.2, CONNECTOR:CONN-HOLE-1.2, F.Cu at (101.6, 109.2)
- added VAL**: CONN-HOLE-1.2, CONNECTOR:CONN-HOLE-1.2, F.Cu at (61.0, 63.5)
- added VAL**: CONN-HOLE-1.2, CONNECTOR:CONN-HOLE-1.2, F.Cu at (63.5, 63.5)
- added VAL**: CONN-HOLE-1.2, CONNECTOR:CONN-HOLE-1.2, F.Cu at (53.3, 63.5)
- added VAL**: CONN-HOLE-1.2, CONNECTOR:CONN-HOLE-1.2, F.Cu at (55.9, 63.5)
- added VAL**: CONN-HOLE-1.2, CONNECTOR:CONN-HOLE-1.2, F.Cu at (58.4, 58.4)
- added VAL**: CONN-HOLE-1.2, CONNECTOR:CONN-HOLE-1.2, F.Cu at (58.4, 61.0)
- added VAL**: CONN-HOLE-1.2, CONNECTOR:CONN-HOLE-1.2, F.Cu at (58.4, 66.0)
- added VAL**: CONN-HOLE-1.2, CONNECTOR:CONN-HOLE-1.2, F.Cu at (53.3, 109.2)
- added VAL**: CONN-HOLE-1.2, CONNECTOR:CONN-HOLE-1.2, F.Cu at (61.0, 66.0)
- added VAL**: CONN-HOLE-1.2, CONNECTOR:CONN-HOLE-1.2, F.Cu at (63.5, 58.4)
- added VAL**: CONN-HOLE-1.2, CONNECTOR:CONN-HOLE-1.2, F.Cu at (61.0, 58.4)
- added VAL**: CONN-HOLE-1.2, CONNECTOR:CONN-HOLE-1.2, F.Cu at (68.6, 63.5)
- added VAL**: CONN-HOLE-1.2, CONNECTOR:CONN-HOLE-1.2, F.Cu at (68.6, 61.0)
- added VAL**: CONN-HOLE-1.2, CONNECTOR:CONN-HOLE-1.2, F.Cu at (68.6, 66.0)
- added VAL**: CONN-HOLE-1.2, CONNECTOR:CONN-HOLE-1.2, F.Cu at (66.0, 66.0)
- added VAL**: CONN-HOLE-1.2, CONNECTOR:CONN-HOLE-1.2, F.Cu at (66.0, 63.5)
- added VAL**: CONN-HOLE-1.2, CONNECTOR:CONN-HOLE-1.2, F.Cu at (68.6, 58.4)
- added VAL**: CONN-HOLE-1.2, CONNECTOR:CONN-HOLE-1.2, F.Cu at (66.0, 61.0)
- added VAL**: CONN-HOLE-1.2, CONNECTOR:CONN-HOLE-1.2, F.Cu at (53.3, 99.1)
- added VAL**: CONN-HOLE-1.2, CONNECTOR:CONN-HOLE-1.2, F.Cu at (66.0, 58.4)
- added VAL**: CONN-HOLE-1.2, CONNECTOR:CONN-HOLE-1.2, F.Cu at (68.6, 68.6)
- added VAL**: CONN-HOLE-1.2, CONNECTOR:CONN-HOLE-1.2, F.Cu at (61.0, 68.6)
- added VAL**: CONN-HOLE-1.2, CONNECTOR:CONN-HOLE-1.2, F.Cu at (63.5, 68.6)
- added VAL**: CONN-HOLE-1.2, CONNECTOR:CONN-HOLE-1.2, F.Cu at (66.0, 68.6)
- added VAL**: CONN-HOLE-1.2, CONNECTOR:CONN-HOLE-1.2, F.Cu at (61.0, 78.7)
- added VAL**: CONN-HOLE-1.2, CONNECTOR:CONN-HOLE-1.2, F.Cu at (63.5, 76.2)
- added VAL**: CONN-HOLE-1.2, CONNECTOR:CONN-HOLE-1.2, F.Cu at (63.5, 78.7)
- added VAL**: CONN-HOLE-1.2, CONNECTOR:CONN-HOLE-1.2, F.Cu at (66.0, 76.2)
- added VAL**: CONN-HOLE-1.2, CONNECTOR:CONN-HOLE-1.2, F.Cu at (58.4, 78.7)
- added VAL**: CONN-HOLE-1.2, CONNECTOR:CONN-HOLE-1.2, F.Cu at (53.3, 94.0)
- added VAL**: CONN-HOLE-1.2, CONNECTOR:CONN-HOLE-1.2, F.Cu at (58.4, 73.7)
- added VAL**: CONN-HOLE-1.2, CONNECTOR:CONN-HOLE-1.2, F.Cu at (58.4, 76.2)
- added VAL**: CONN-HOLE-1.2, CONNECTOR:CONN-HOLE-1.2, F.Cu at (58.4, 68.6)
- added VAL**: CONN-HOLE-1.2, CONNECTOR:CONN-HOLE-1.2, F.Cu at (58.4, 71.1)
- added VAL**: CONN-HOLE-1.2, CONNECTOR:CONN-HOLE-1.2, F.Cu at (61.0, 71.1)
- added VAL**: CONN-HOLE-1.2, CONNECTOR:CONN-HOLE-1.2, F.Cu at (63.5, 71.1)
- added VAL**: CONN-HOLE-1.2, CONNECTOR:CONN-HOLE-1.2, F.Cu at (66.0, 71.1)
- added VAL**: CONN-HOLE-1.2, CONNECTOR:CONN-HOLE-1.2, F.Cu at (66.0, 73.7)
- added VAL**: CONN-HOLE-1.2, CONNECTOR:CONN-HOLE-1.2, F.Cu at (63.5, 73.7)
- added VAL**: CONN-HOLE-1.2, CONNECTOR:CONN-HOLE-1.2, F.Cu at (68.6, 76.2)
- added VAL**: CONN-HOLE-1.2, CONNECTOR:CONN-HOLE-1.2, F.Cu at (53.3, 96.5)
- added VAL**: CONN-HOLE-1.2, CONNECTOR:CONN-HOLE-1.2, F.Cu at (68.6, 73.7)
- added VAL**: CONN-HOLE-1.2, CONNECTOR:CONN-HOLE-1.2, F.Cu at (68.6, 71.1)
- added VAL**: CONN-HOLE-1.2, CONNECTOR:CONN-HOLE-1.2, F.Cu at (68.6, 78.7)
- added VAL**: CONN-HOLE-1.2, CONNECTOR:CONN-HOLE-1.2, F.Cu at (66.0, 81.3)
- added VAL**: CONN-HOLE-1.2, CONNECTOR:CONN-HOLE-1.2, F.Cu at (66.0, 78.7)
- added VAL**: CONN-HOLE-1.2, CONNECTOR:CONN-HOLE-1.2, F.Cu at (61.0, 76.2)
- added VAL**: CONN-HOLE-1.2, CONNECTOR:CONN-HOLE-1.2, F.Cu at (61.0, 73.7)
- added VAL**: CONN-HOLE-1.2, CONNECTOR:CONN-HOLE-1.2, F.Cu at (58.4, 83.8)
- added VAL**: CONN-HOLE-1.2, CONNECTOR:CONN-HOLE-1.2, F.Cu at (61.0, 83.8)
- added VAL**: CONN-HOLE-1.2, CONNECTOR:CONN-HOLE-1.2, F.Cu at (68.6, 81.3)
- added VAL**: CONN-HOLE-1.2, CONNECTOR:CONN-HOLE-1.2, F.Cu at (55.9, 104.1)
- added VAL**: CONN-HOLE-1.2, CONNECTOR:CONN-HOLE-1.2, F.Cu at (68.6, 83.8)
- added VAL**: CONN-HOLE-1.2, CONNECTOR:CONN-HOLE-1.2, F.Cu at (61.0, 81.3)
- added VAL**: CONN-HOLE-1.2, CONNECTOR:CONN-HOLE-1.2, F.Cu at (58.4, 81.3)
- added VAL**: CONN-HOLE-1.2, CONNECTOR:CONN-HOLE-1.2, F.Cu at (63.5, 81.3)
- added VAL**: CONN-HOLE-1.2, CONNECTOR:CONN-HOLE-1.2, F.Cu at (66.0, 83.8)
- added VAL**: CONN-HOLE-1.2, CONNECTOR:CONN-HOLE-1.2, F.Cu at (63.5, 83.8)
- added VAL**: CONN-HOLE-1.2, CONNECTOR:CONN-HOLE-1.2, F.Cu at (61.0, 86.4)
- added VAL**: CONN-HOLE-1.2, CONNECTOR:CONN-HOLE-1.2, F.Cu at (58.4, 86.4)
- added VAL**: CONN-HOLE-1.2, CONNECTOR:CONN-HOLE-1.2, F.Cu at (58.4, 88.9)
- added VAL**: CONN-HOLE-1.2, CONNECTOR:CONN-HOLE-1.2, F.Cu at (58.4, 91.4)
- moved C6 99.4 mm to (182.6, 95.6)
- moved R5 98.7 mm to (181.2, 101.0), turned to 90 degrees
- moved R4 93.0 mm to (192.1, 87.3)
- moved R8 88.9 mm to (192.1, 92.9), turned to 180 degrees
- moved C4 87.4 mm to (185.0, 102.3), turned to 180 degrees
- moved DL1 87.0 mm to (195.1, 89.3)
- moved DL3 85.0 mm to (195.1, 92.9)
- moved C2 82.0 mm to (188.2, 96.8), turned to 90 degrees
- moved DL2 81.2 mm to (195.1, 87.3)
- moved P1 28.5 mm to (194.3, 99.6)
- moved C5 27.0 mm to (190.2, 79.1)
- moved C1 27.0 mm to (191.6, 77.9)
- moved C3 27.0 mm to (191.6, 74.3)
- moved DL4 27.0 mm to (195.5, 81.8)
- moved DL5 27.0 mm to (195.5, 83.8)
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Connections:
- BRD1 pad 30: (no net) -> /TX
- BRD1 pad 32: (no net) -> /RX
- C4 pad 1: (no net) -> Net-(C4-Pad1)
- DL1 pad 2: (no net) -> Net-(DL1-Pad2)
- DL2 pad 2: (no net) -> Net-(DL2-Pad2)
- L1 pad 1: (no net) -> Net-(L1-Pad1)
- R5 pad 2: (no net) -> Net-(R5-Pad2)
- U2 pad 1: (no net) -> Net-(J1-Pad1)
- U2 pad 4: (no net) -> Net-(J2-Pad1)
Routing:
- net /VIN: track 0.00 -> 194.6 mm, vias 0 -> 3
- net +3.3V: track 0.00 -> 164.4 mm, vias 0 -> 3
- net GND: track 1.70 -> 139.9 mm, vias 0 -> 2
- net (no net): track 0.00 -> 101.6 mm
- net /RX: track 0.00 -> 92.4 mm
- net /TX: track 0.00 -> 88.1 mm
- net /VCCIO: track 16.0 -> 38.0 mm, vias 0 -> 3
- net Net-(R7-Pad1): track 0.00 -> 20.6 mm
- net /VUSB: track 0.00 -> 17.0 mm
- net Net-(DL1-Pad2): track 0.00 -> 8.70 mm, vias 0 -> 1
- net Net-(DL2-Pad2): track 0.00 -> 8.48 mm, vias 0 -> 1
- net Net-(R6-Pad2): track 0.00 -> 6.29 mm, vias 0 -> 2
- net Net-(C4-Pad1): track 0.00 -> 2.72 mm
- net Net-(J1-Pad1): track 0.00 -> 2.41 mm
- net Net-(J2-Pad1): track 0.00 -> 2.41 mm
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- added copper zone on F.Cu, net /VEXT
- added copper zone on F.Cu, net /VIN
- added copper zone on B.Cu, net GND
- added copper zone on F.Cu, net GND
- added copper zone on F.Cu, net Net-(D1-Pad1)
- added copper zone on F.Cu, net Net-(L1-Pad1)
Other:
- board text added: "3V3"
- board text added: "5V"
- board text added: "GND"
- board text added: "L1"
- board text added: "L2"

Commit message: Added fiducials, logo and license.
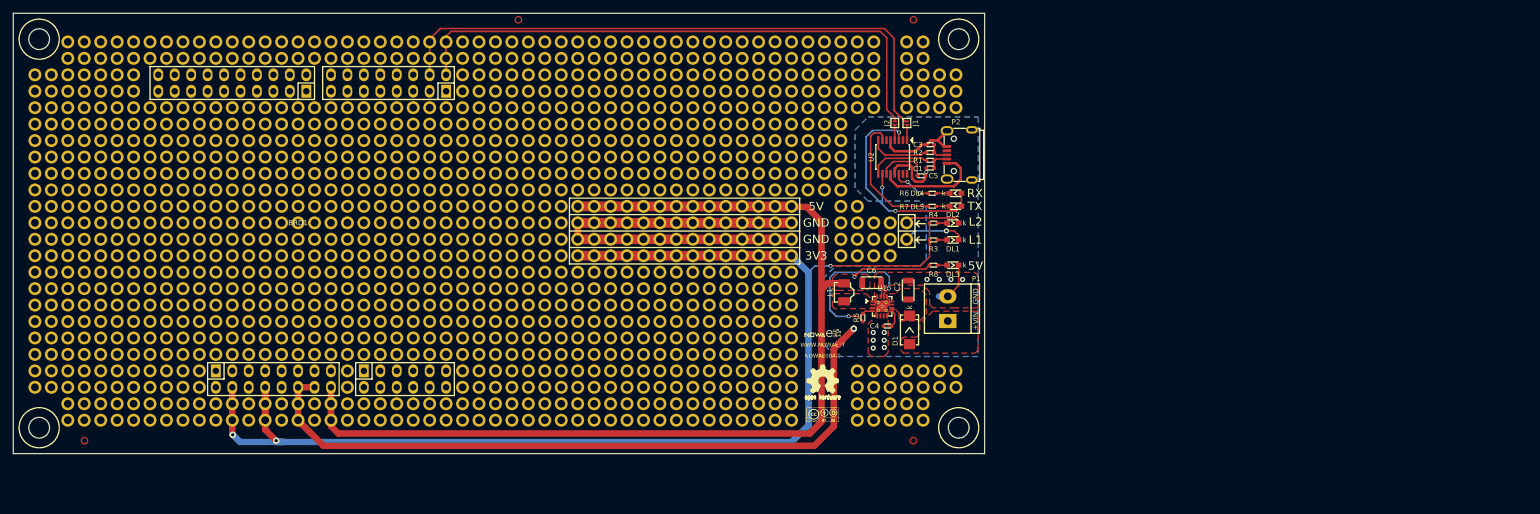
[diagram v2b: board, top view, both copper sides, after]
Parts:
- added G***: LOGO, LOGO:LOGO, F.Cu at (175.0, 103.3)
- added G***: LOGO, LOGO:Logo_silk_CC-BY-SA_5x2mm, F.Cu at (175.0, 116.0)
- added G***: LOGO, LOGO:Logo_silk_OSHW_6x6mm, F.Cu at (175.0, 110.5)
- added VAL**: FIDUCIAL-TOP, MECHANICAL:FIDUCIAL-TOP, F.Cu at (61.0, 120.0)
- added VAL**: FIDUCIAL-TOP, MECHANICAL:FIDUCIAL-TOP, F.Cu at (128.0, 55.0)
- added VAL**: FIDUCIAL-TOP, MECHANICAL:FIDUCIAL-TOP, F.Cu at (189.0, 120.0)
- added VAL**: FIDUCIAL-TOP, MECHANICAL:FIDUCIAL-TOP, F.Cu at (189.0, 55.0)
- moved DL2 0.89 mm to (195.1, 86.4)
- moved R4 0.89 mm to (192.1, 86.4)
- moved DL1 0.30 mm to (195.1, 89.0)
- moved R3 0.30 mm to (192.1, 89.0)
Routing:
- net GND: track 139.9 -> 143.3 mm
- net Net-(DL1-Pad2): track 8.70 -> 11.3 mm
- net +3.3V: track 164.4 -> 165.7 mm
- net Net-(DL2-Pad2): track 8.48 -> 8.95 mm, vias 1 -> 0
- net (no net): vias 0 -> 10
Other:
- board text added: "NOWAE004-0"
- board text added: "WWW.NOWAE.IT"
